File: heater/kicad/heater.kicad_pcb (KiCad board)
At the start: 2 copper layers, 90 x 88.4 mm, 82 parts, among them J1 Conn_01x02_Pin, J2 Conn_01x02_Pin, J5 pcie_98, U1 OPA863SIDBVR, U10 B0509XT-1WR3, U11 OPA863SIDBVR, U12 OPA863SIDBVR, U13 OPA863SIDBVR, U15 LTC1968, U2 ESD5344D-TP, U3 LP2985-5.0, U4 ESD5344D-TP, U5 ISO1541, U6 LTC1968, U8 ADS1115IDGS, U9 XC6206P332MR

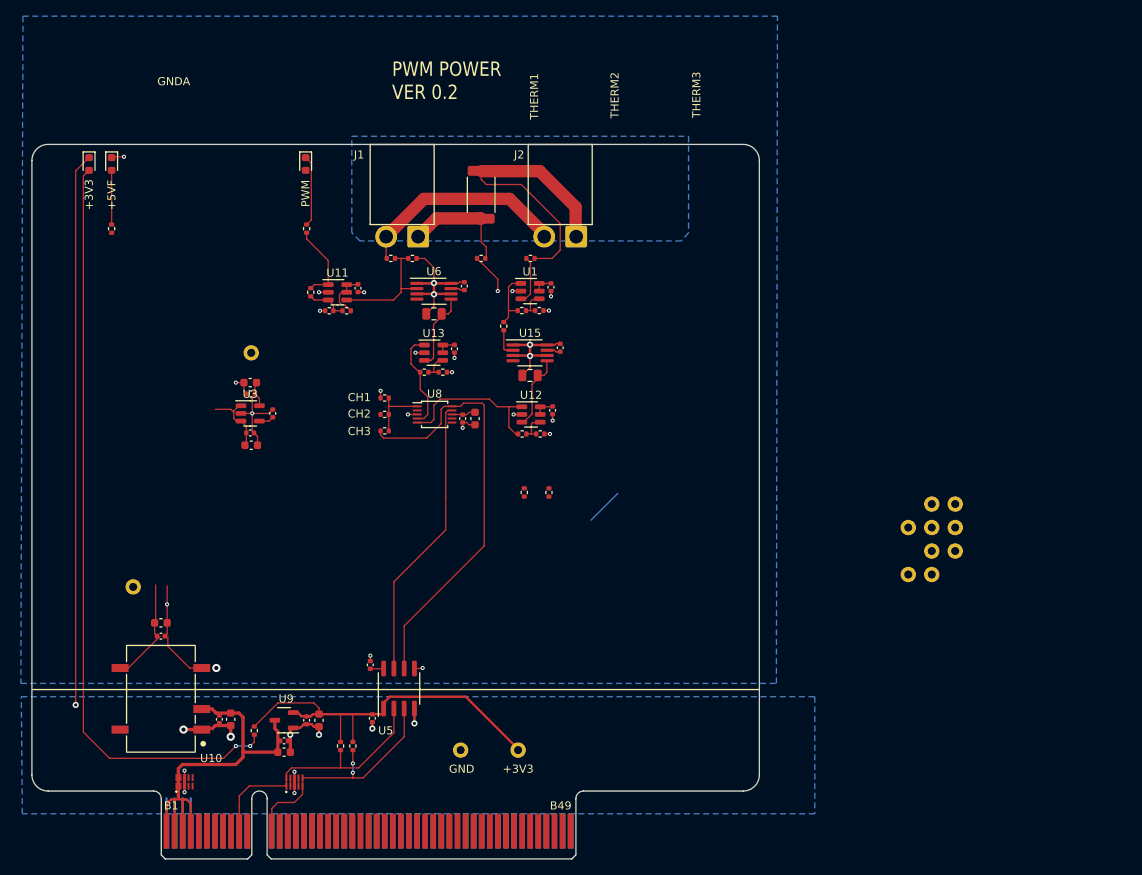
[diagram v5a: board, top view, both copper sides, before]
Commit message: Heater layout work in progress. Passing all DRCs.
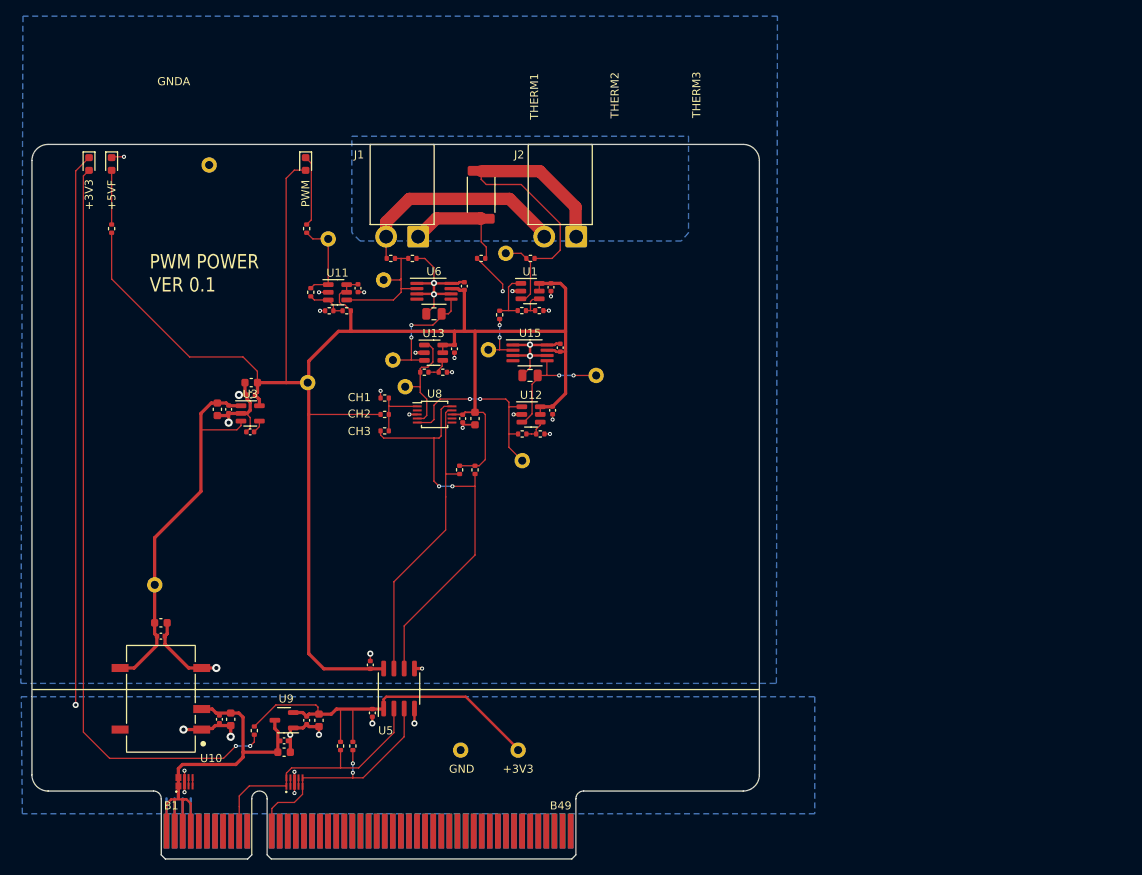
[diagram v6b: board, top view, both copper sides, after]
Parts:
- moved TP10 101.4 mm to (-6.22, -85.9)
- moved TP9 82.8 mm to (8.51, -76.7)
- moved TP12 76.0 mm to (15.4, -71.6)
- moved TP13 72.6 mm to (16.5, -61.7)
- moved TP14 71.0 mm to (18.0, -58.4)
- moved TP11 61.5 mm to (28.3, -63.0)
- moved TP8 61.2 mm to (30.5, -74.9)
- moved TP3 48.5 mm to (32.5, -49.3)
- moved TP5 45.8 mm to (41.7, -59.8)
- moved R8 9.56 mm to (26.7, -48.1), turned to 90 degrees
- moved R7 8.48 mm to (24.8, -48.1), turned to 90 degrees
- moved TP7 7.90 mm to (5.97, -58.9)
- moved C26 6.11 mm to (-5.21, -55.6), turned to 90 degrees
- moved C24 3.96 mm to (-3.81, -55.6), turned to 90 degrees
- moved C20 3.61 mm to (-1.14, -52.8), turned to 0 degrees
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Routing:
- net +5VF: track 25.3 -> 223.9 mm
- net /9VF: track 22.0 -> 48.3 mm
- net GNDF: track 87.4 -> 79.9 mm, vias 27 -> 26
- net Net-(U12-+): track 9.09 -> 15.4 mm, vias 0 -> 2
- net Net-(U13-+): track 9.53 -> 15.1 mm, vias 0 -> 2
- net Net-(U8-AIN1): track 19.8 -> 24.4 mm, vias 0 -> 2
- net Net-(U15-IN1): track 3.50 -> 6.87 mm, vias 0 -> 2
- net Net-(U1-+): track 6.03 -> 8.83 mm
- net Net-(U11--): track 14.9 -> 17.1 mm
- net Net-(U8-AIN0): track 12.3 -> 14.1 mm
- net Net-(U5-SDA2): track 35.3 -> 37.0 mm
- net Net-(U5-SCL2): track 53.1 -> 51.4 mm, vias 0 -> 2
- net +3V3: track 48.7 -> 50.2 mm
- net Net-(R22-Pad1): track 9.87 -> 11.0 mm
- net Net-(J1-Pin_2): track 26.3 -> 27.4 mm
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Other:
- board text added: "PWM POWER VER 0.1"
- board text removed: "PWM POWER VER 0.2"

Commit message: Work in progress. Tweaked the heater layout.
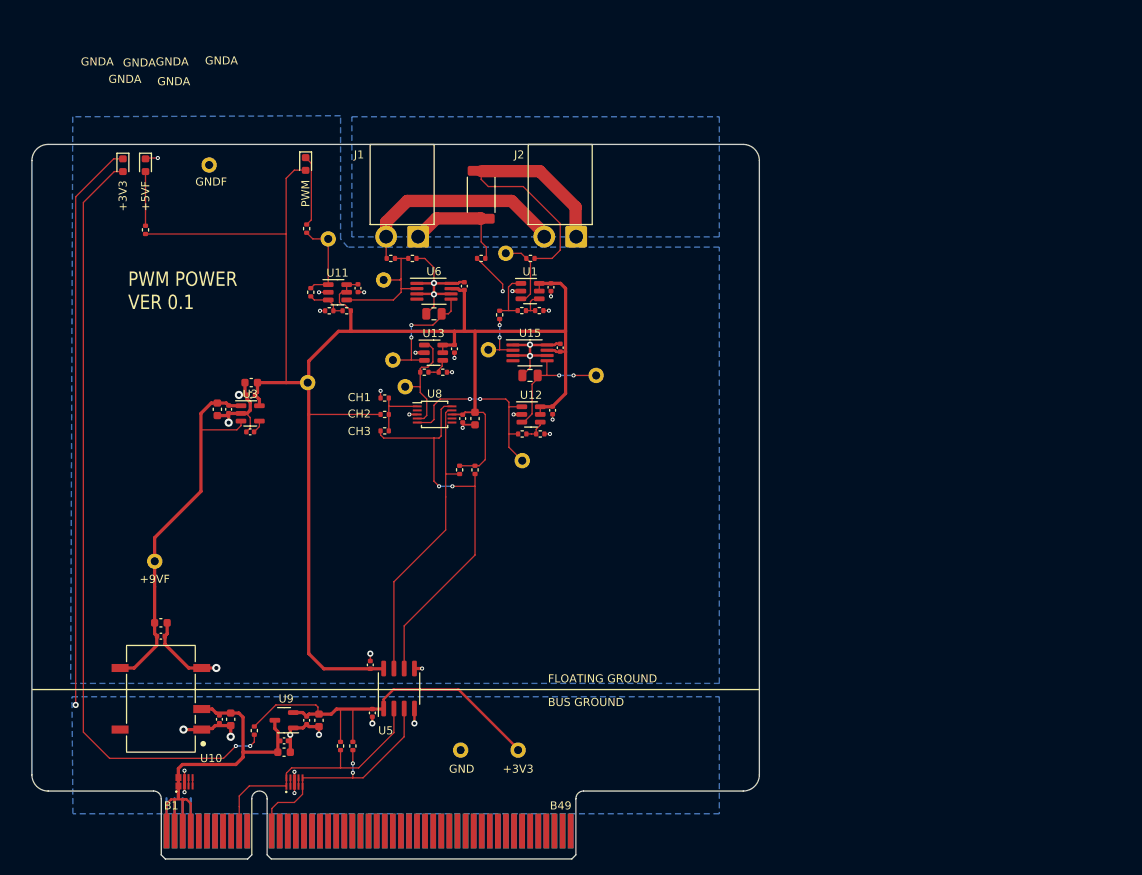
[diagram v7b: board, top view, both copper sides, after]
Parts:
- R4: value 0R025 50ppm 3W -> 0R025 50ppm
- moved D2 4.19 mm to (-16.9, -85.8)
- moved D5 4.19 mm to (-14.1, -85.8)
- moved R27 4.19 mm to (-14.1, -77.8)
- moved TP4 2.92 mm to (-13.0, -36.8)
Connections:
- net Net-(J1-Pin_2) renamed /VIN+
- U15 pad 4: (no net) -> unconnected-(U15-NC-Pad4)
- U6 pad 4: (no net) -> unconnected-(U6-NC-Pad4)
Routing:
- net +5VF: track 223.9 -> 211.4 mm
- net GND: track 107.6 -> 109.8 mm
- net Net-(D2-A): track 94.0 -> 96.2 mm
- net +3V3: track 50.2 -> 51.0 mm
- added copper zone on B.Cu, net /VIN+
- removed copper zone on B.Cu, net (none)
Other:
- board text added: "+9VF"
- board text added: "BUS GROUND"
- board text added: "FLOATING GROUND"
- board text added: "GNDF"
- board text removed: "THERM1"
- board text removed: "THERM2"
- board text removed: "THERM3"

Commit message: Work in progress. Added silkscreen labels to the heater layout.
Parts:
- moved TP5 0.76 mm to (8.51, -77.5)
- renumbered C6 to C1, C27 to C10, C20 to C11, C21 to C12, C15 to C13, C24 to C14, C26 to C15, C9 to C16, C19 to C17, C16 to C18, C10 to C19, C11 to C2, C18 to C20, C4 to C21, C14 to C22, C3 to C23, C2 to C24, C1 to C25, C12 to C3, C7 to C4, C13 to C5, C5 to C6, C17 to C7, C28 to C9, D5 to D1, D1 to D2, D2 to D3, J5 to J3, R23 to R1, R2 to R10, R24 to R11, R6 to R12, R22 to R13, R17 to R14, R18 to R15, R3 to R16, R5 to R17, R13 to R18, R16 to R19, R4 to R2, R14 to R20, R7 to R21, R8 to R22, R9 to R23, R10 to R24, R15 to R25, R19 to R3, R20 to R4, R27 to R5, R21 to R6, R11 to R7, R12 to R8, R1 to R9, TP10 to TP1, TP3 to TP10, TP4 to TP11, TP2 to TP12, TP1 to TP13, TP8 to TP2, TP12 to TP3, TP11 to TP4, TP9 to TP5, TP13 to TP6, TP5 to TP7, TP7 to TP8, TP14 to TP9, U2 to U11, U4 to U12, U9 to U13, U11 to U2, U6 to U3, U15 to U4, U13 to U5, U12 to U6, U3 to U7, U5 to U9
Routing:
- net /9VF: track 48.3 -> 50.5 mm
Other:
- board text added: "TP10"
- board text added: "TP4"
- board text added: "TP5"
- board text added: "TP7"
